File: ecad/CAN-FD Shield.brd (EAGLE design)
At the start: 68.8 x 53.5 mm, 40 parts, among them J2 JUMPER-3P-SHORT, J3 JUMPER-3P-SHORT, J4 JUMPER-3P-SHORT, J5 JUMPER-3P-SHORT, Q1 BSS123, U5 MCP2517FD, U6 MCP2542, X2 20MHz

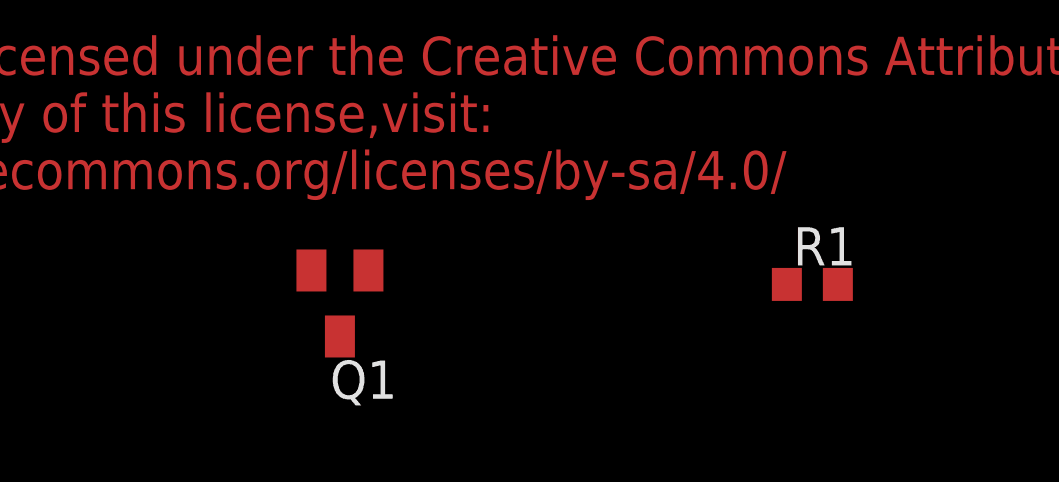
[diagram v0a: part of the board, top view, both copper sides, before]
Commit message: failure generator added to hardware design
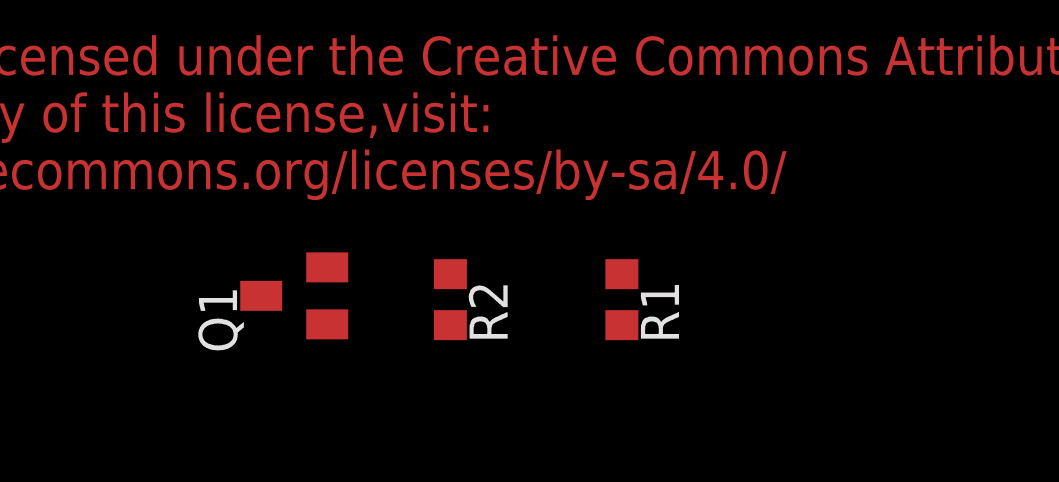
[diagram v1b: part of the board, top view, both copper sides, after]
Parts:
- added R2: 100k, rcl:R0603
- Q1: value BSS123 -> FDV303
- moved R1 6.37 mm to (30.9, -11.2), turned to 270 degrees
- moved Q1 1.55 mm to (19.9, -11.0), turned to 90 degrees
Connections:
- new net SOF: R1.1, U5.3
- net GND: now also R2.1
- net IO7: now also R2.2
- net RX_CAN: no longer R1.1
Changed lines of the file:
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@@
 </element>
 <element name="U$1" library="Longan-LOGO" package="LONGAN-SILK-SMALLER" value="" x="45.212" y="18.923" rot="MR0"/>
-<element name="R1" library="rcl" package="R0603" value="0" x="37.211" y="-10.668"/>
-<element name="Q1" library="transistor-small-signal" package="SOT23" value="BSS123" x="21.463" y="-11.303" rot="R180"/>
+<element name="R1" library="rcl" package="R0603" value="0" x="30.861" y="-11.176" rot="R270"/>
+<element name="Q1" library="transistor-small-signal" package="SOT23" value="FDV303" x="19.939" y="-11.049" rot="R90"/>
+<element name="R2" library="rcl" package="R0603" value="100k" x="25.146" y="-11.176" rot="R270"/>
 </elements>
 <signals>
@@
 <contactref element="C1" pad="1"/>
 <contactref element="Q1" pad="2"/>
-<wire x1="25.4" y1="10.16" x2="20.513" y2="-10.203" width="0" layer="19" extent="1-1"/>
+<contactref element="R2" pad="1"/>
+<wire x1="25.146" y1="-10.326" x2="21.039" y2="-10.099" width="0" layer="19" extent="1-1"/>
+<wire x1="40.64" y1="2.54" x2="25.146" y2="-10.326" width="0" layer="19" extent="1-1"/>
 </signal>
 <signal name="5V">
@@
 <wire x1="21.463" y1="25.273" x2="20.16" y2="25.273" width="0.2032" layer="1"/>
 <contactref element="Q1" pad="3"/>
-<wire x1="21.463" y1="-12.403" x2="20.407" y2="4.445" width="0" layer="19" extent="1-1"/>
+<wire x1="18.839" y1="-11.049" x2="20.193" y2="4.445" width="0" layer="19" extent="1-1"/>
 </signal>
 <signal name="TX_CAN">
@@
 <wire x1="28.575" y1="28.194" x2="25.941" y2="28.194" width="0.2032" layer="1"/>
 <wire x1="25.941" y1="28.194" x2="25.56" y2="27.813" width="0.2032" layer="1"/>
-<contactref element="R1" pad="1"/>
-<wire x1="34.036" y1="21.336" x2="36.361" y2="-10.668" width="0" layer="19" extent="1-1"/>
 </signal>
 <signal name="ADC1">
@@
 <contactref element="U4" pad="8"/>
 <contactref element="Q1" pad="1"/>
-<wire x1="22.413" y1="-10.203" x2="45.72" y2="50.8" width="0" layer="19" extent="1-1"/>
+<contactref element="R2" pad="2"/>
+<wire x1="25.146" y1="-12.026" x2="45.72" y2="50.8" width="0" layer="19" extent="1-1"/>
+<wire x1="21.039" y1="-11.999" x2="25.146" y2="-12.026" width="0" layer="19" extent="1-1"/>
 </signal>
 <signal name="ADC7">
@@
 <wire x1="52.07" y1="46.99" x2="55.88" y2="50.8" width="0.2032" layer="1"/>
 <contactref element="R1" pad="2"/>
-<wire x1="38.061" y1="-10.668" x2="37.719" y2="30.861" width="0" layer="19" extent="1-16"/>
+<wire x1="30.861" y1="-12.026" x2="36.957" y2="30.861" width="0" layer="19" extent="1-16"/>
 </signal>
 <signal name="SCL">
@@
 <wire x1="27.94" y1="15.875" x2="25.908" y2="13.843" width="0.4064" layer="1"/>
 </signal>
+<signal name="SOF">
+<contactref element="R1" pad="1"/>
+<contactref element="U5" pad="3"/>
+<wire x1="30.861" y1="-10.326" x2="34.036" y2="20.066" width="0" layer="19" extent="1-1"/>
+</signal>
 </signals>
